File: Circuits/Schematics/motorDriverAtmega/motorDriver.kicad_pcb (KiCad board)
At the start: 2 copper layers, 42 x 42 mm, 19 parts, among them J1 Conn_01x04_Pin, J2 Conn_01x02_Pin, J3 Conn_01x03_Pin, J6 Conn_02x03_Counter_Clockwise, U1 MAX485E, U3 ATmega328P-A, Y2 Crystal_GND24

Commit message: Main PCB Sketches
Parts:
- J3: value Conn_01x03_Pin -> Screw_Terminal_01x03; footprint TerminalBlock_Phoenix:TerminalBlock_Phoenix_MKDS-1,5-3-5.08_1x03_P5.08mm_Horizontal -> TerminalBlock_Phoenix:TerminalBlock_Phoenix_PT-1,5-3-5.0-H_1x03_P5.00mm_Horizontal
- moved R1 23.4 mm to (123.6, 50.6), turned to -90 degrees
- moved C10 15.3 mm to (105.7, 68.4), turned to 180 degrees
- moved R3 15.1 mm to (113.5, 68.0), turned to 0 degrees
- moved C11 14.2 mm to (123.6, 68.2)
- moved C14 0.95 mm to (106.2, 62.1)
- moved J3 0.61 mm to (95.8, 77.3)
- moved C12 0.60 mm to (123.7, 60.9)
- moved J2 0.08 mm to (110.5, 52.1)
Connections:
- net Net-(J2-Pin_1) renamed /RS-485 A
- net Net-(J2-Pin_2) renamed /RS-485 B
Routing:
- net GND: track 168.5 -> 183.7 mm, vias 0 -> 1
- net +5V: track 100.2 -> 94.4 mm, vias 2 -> 3
- net Net-(U1-DE): track 11.0 -> 16.4 mm
- net Net-(J6-Pin_3): track 20.4 -> 24.4 mm, vias 1 -> 2
- net Net-(U3-XTAL2/PB7): track 8.72 -> 7.75 mm

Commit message: PCB Updates
Şematikler temize çekildi.
motorDriverAtmega hatalı RS-485 DE (pin 3) bağlantısı düzeltildi.
masterController şematiği tamamlandı.
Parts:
- renumbered C8 to C1, C10 to C2, C11 to C3, C12 to C4, C13 to C5, C14 to C6, C4 to C7, C3 to C8, J6 to J1, J3 to J2, J1 to J3, R3 to R1, R1 to R2, U3 to U1, U1 to U2, Y2 to Y1
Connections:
- A1 pad 3: /MTR_A1 -> /MTR_A2
- A1 pad 4: /MTR_A2 -> /MTR_A1
- R2 pad 1: Net-(U1-DE) -> Net-(U2-~{RE})
- U1 pad 32: unconnected-(U3-PD2-Pad32) -> /Transmit
- U2 pad 2: Net-(U1-DE) -> Net-(U2-~{RE})
- U2 pad 3: Net-(U1-DE) -> /Transmit
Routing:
- net Net-(U1-DE): track 16.4 -> 0.00 mm
- net Net-(U2-~{RE}): track 0.00 -> 14.8 mm
- net /Transmit: track 0.00 -> 14.7 mm, vias 0 -> 2
- net /MTR_A2: track 6.85 -> 9.97 mm
- net +5V: track 94.4 -> 92.6 mm
- net /MTR_A1: track 6.73 -> 5.56 mm

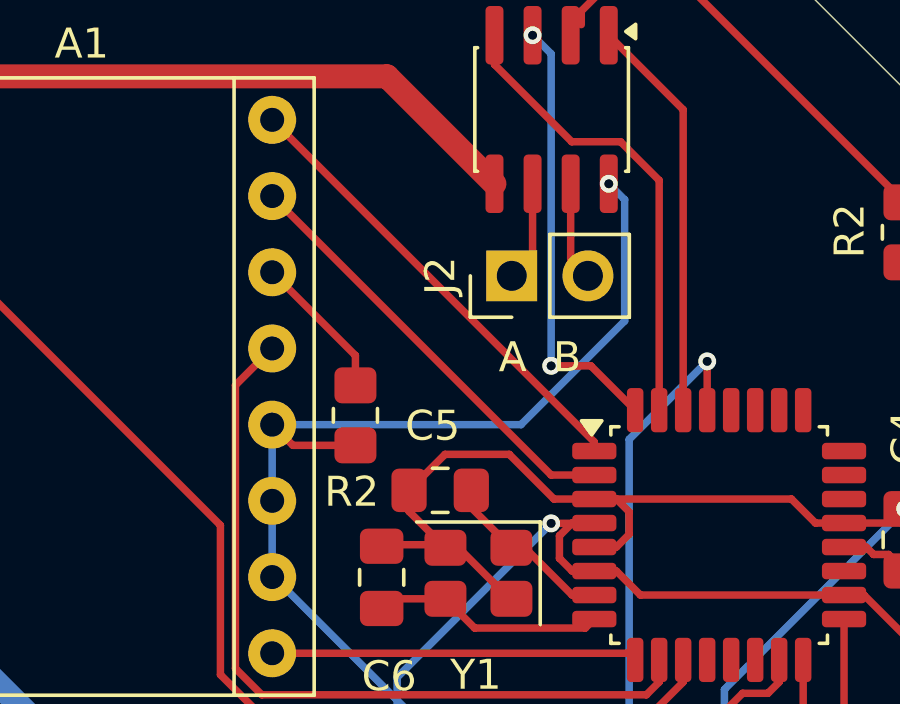
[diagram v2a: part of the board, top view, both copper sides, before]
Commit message: Bug fixes, footprint assignments
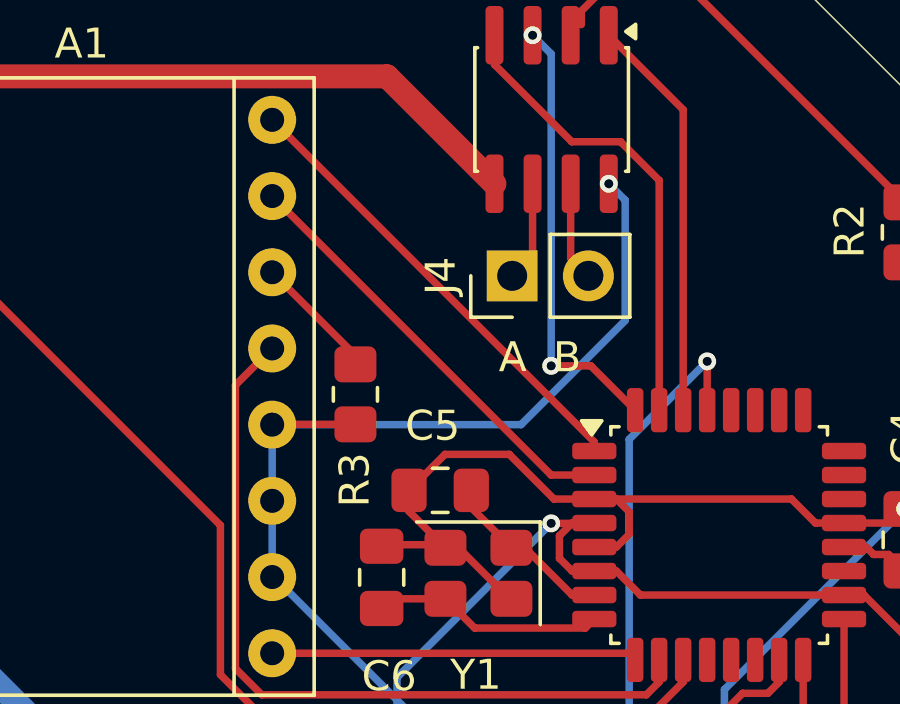
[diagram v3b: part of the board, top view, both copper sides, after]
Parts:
- removed the J2 at (110.5, 52.1)
- removed the R2 at (105.3, 56.8)
- added J4: Conn_01x02_Pin, Connector_PinHeader_2.54mm:PinHeader_1x02_P2.54mm_Vertical, F.Cu at (110.5, 52.1)
- added R3: 10k, Resistor_SMD:R_0805_2012Metric_Pad1.20x1.40mm_HandSolder, F.Cu at (105.3, 56.0)
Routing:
- net Net-(A1-~{SLP}): track 4.92 -> 4.22 mm

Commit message: Main Controller PCB Completed
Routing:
- net +5V: track 92.4 -> 82.2 mm
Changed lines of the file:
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@@
 		(capping no)
 		(filling no)
+		(zone_defaults)
 		(pcbplotparams
 			(layerselection 0x00000000_00000000_55555555_575555ff)
@@
 	)
 	(segment
-		(start 106.7125 68.425)
-		(end 106.7125 65.4875)
-		(width 0.25)
-		(layer "B.Cu")
-		(net "+5V")
-	)
-	(segment
 		(start 102.55 62.14)
 		(end 102.61 62.14)
@@
 		(width 0.25)
 		(layer "B.Cu")
-		(net "+5V")
-	)
-	(segment
-		(start 106.7125 65.4875)
-		(end 111.85 60.35)
-		(width 0.25)
-		(layer "B.Cu")
